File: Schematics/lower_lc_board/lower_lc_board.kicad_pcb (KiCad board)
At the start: 4 copper layers, 69.5 x 60 mm, 156 parts, among them J1 Conn_01x06, J10 SOL_CONN, J2 SWD_CONN, J3 USB_C_CONN, J4 HALL-1, J5 HALL-2, J6 PT1, J7 Screw_Terminal_01x02, J8 PT1, J9 SOL_CONN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

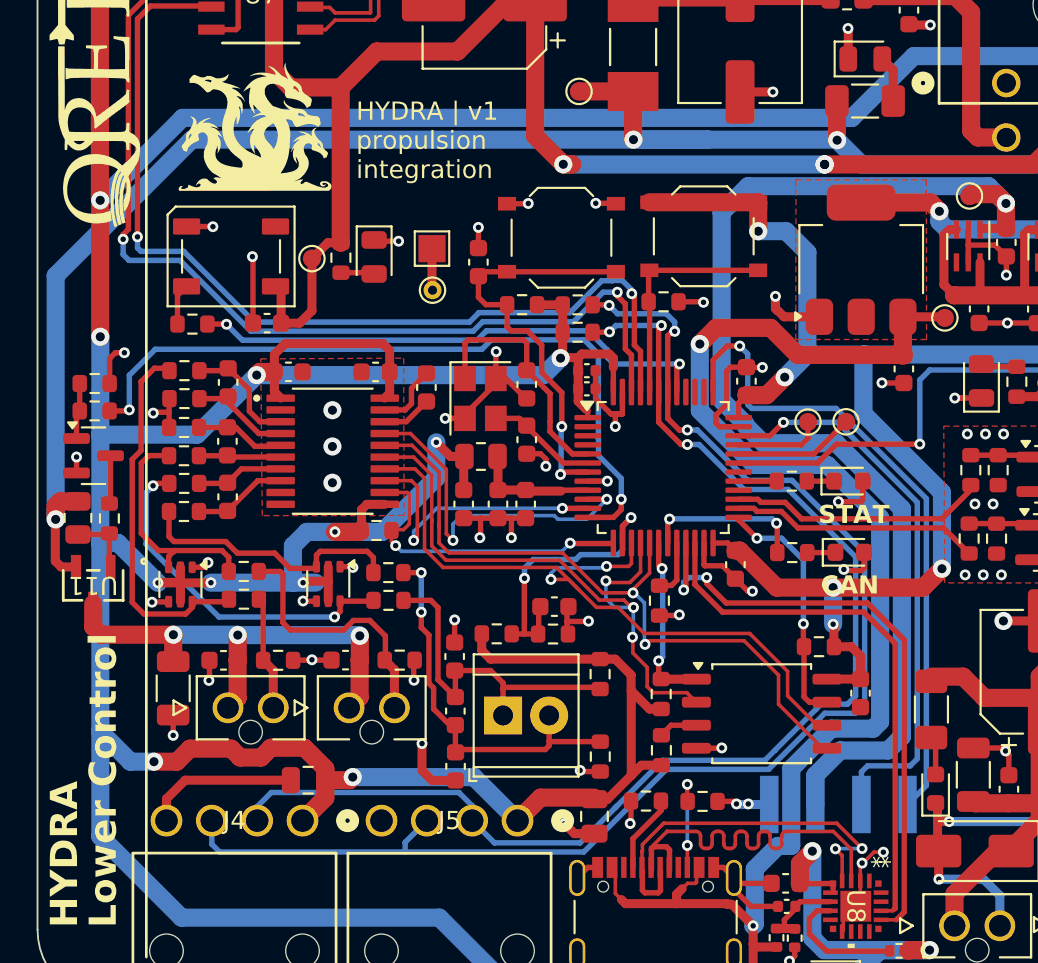
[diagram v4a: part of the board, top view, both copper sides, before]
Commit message: update with new TC screw terminal
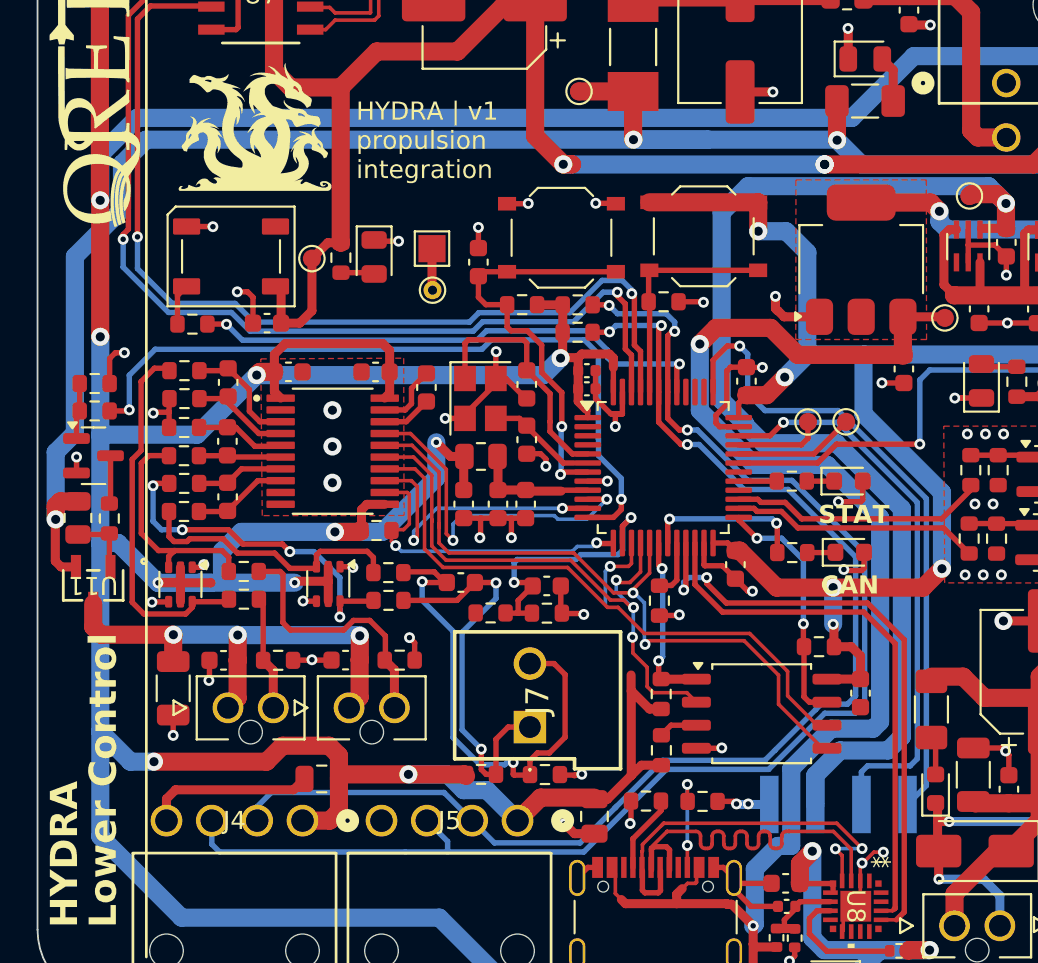
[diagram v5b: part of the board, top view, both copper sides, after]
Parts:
- removed C31, C32: 1nF, Capacitor_SMD:C_0603_1608Metric
- J7: footprint TerminalBlock_TE-Connectivity:TerminalBlock_TE_282834-2_1x02_P2.54mm_Horizontal -> SCREW-VERT:1984769
- moved R26 8.58 mm to (145.1, 95.0), turned to 0 degrees
- moved C30 7.10 mm to (143.9, 84.4), turned to 0 degrees
- moved R27 3.21 mm to (148.6, 95.0), turned to 0 degrees
- moved J7 1.61 mm to (147.8, 92.4), turned to 90 degrees
- moved C34 1.22 mm to (148.7, 84.6)
- moved R25 1.20 mm to (145.6, 86.1)
- moved TH1 1.20 mm to (148.7, 86.1)
- moved C23 0.75 mm to (136.3, 95.2)
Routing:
- net /Sensing Circuitry/TC_N_1: track 21.5 -> 28.0 mm
- net GND: track 173.6 -> 168.3 mm, vias 77 -> 75
- net SPI_SCLK: track 41.2 -> 37.9 mm, vias 2 -> 1
- net /Sensing Circuitry/TC_P_1: track 19.0 -> 22.1 mm, vias 0 -> 2
- net +3V3: track 468.7 -> 471.1 mm, vias 20 -> 19
- net +24V: track 125.9 -> 127.4 mm
- net SPI_MISO: track 34.0 -> 32.5 mm
- net CAN_RX: track 53.0 -> 53.6 mm
- net TEMP_SENSE: track 15.9 -> 15.3 mm
- net Net-(D18A-K3A4): track 19.2 -> 19.4 mm, vias 2 -> 4
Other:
- board text added: "V1.1? notes (2026-03-26) - new power/can/BP entry with molex conn - new molex connectors for solenoids/PTs - restarted design for overall organization - vertical screw term for TC *TODO - get reviewed & adjust - pours - silkscreen"

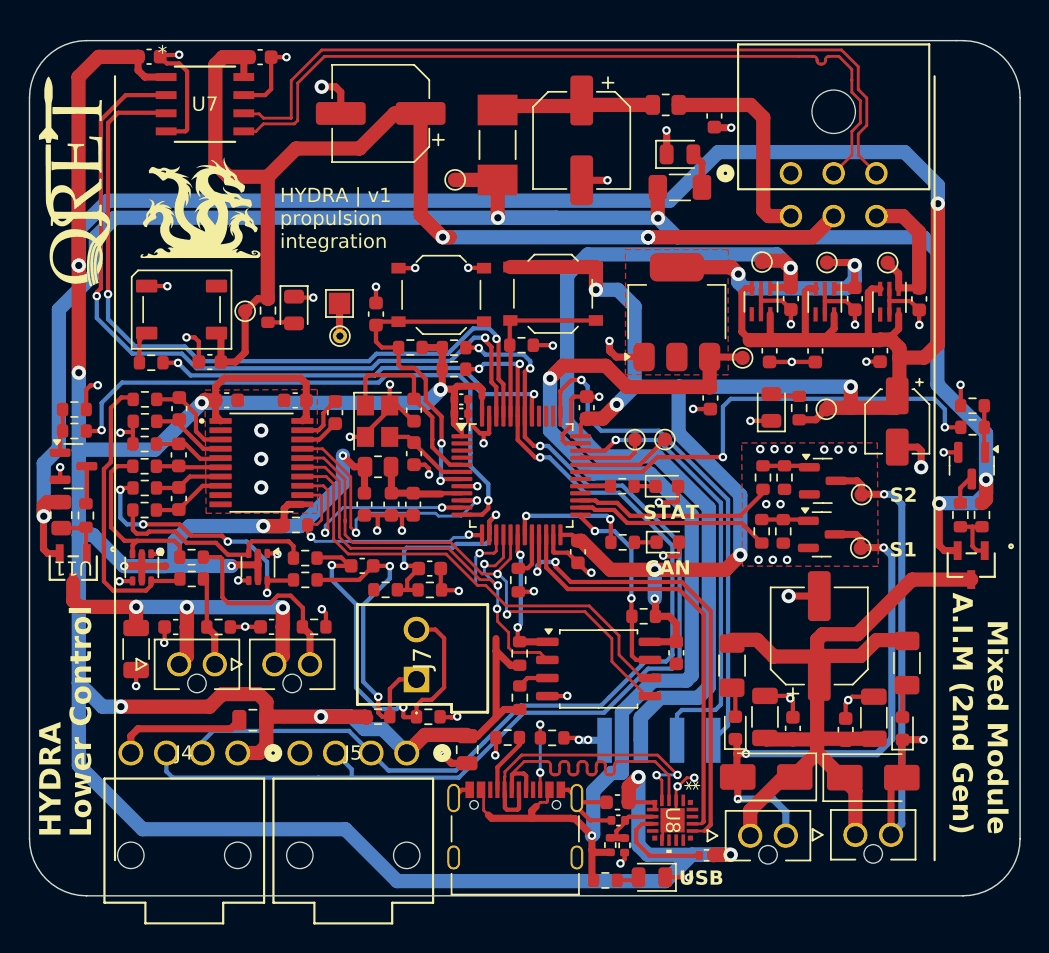
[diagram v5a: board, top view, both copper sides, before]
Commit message: update backplane orientation
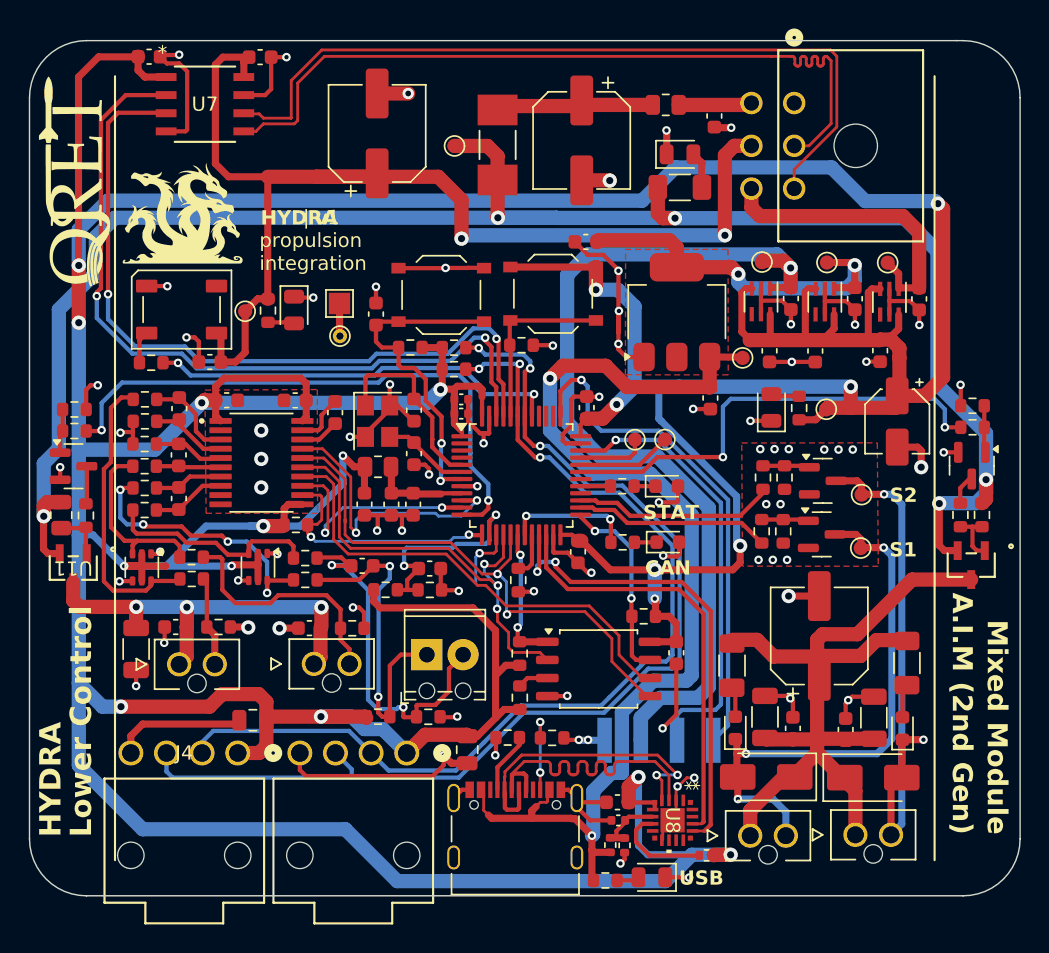
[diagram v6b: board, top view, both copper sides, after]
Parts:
- added C12: 10uF, Capacitor_SMD:C_0603_1608Metric, F.Cu at (159.6, 61.7)
- J7: footprint SCREW-VERT:1984769 -> TerminalBlock_Phoenix:TerminalBlock_Phoenix_MPT-0,5-2-2.54_1x02_P2.54mm_Horizontal
- moved J1 4.94 mm to (174.2, 51.9), turned to 90 degrees
- moved J8 2.77 mm to (140.6, 91.3)
- moved R35 2.68 mm to (143.2, 88.8)
- moved C36 2.66 mm to (140.2, 88.8)
- moved TP1 2.38 mm to (150.4, 54.9)
- moved J7 1.89 mm to (148.5, 90.6), turned to 0 degrees
- moved C4 1.42 mm to (145.0, 54.1), turned to 90 degrees
- moved G*** 1.31 mm to (131.4, 59.7)
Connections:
- net /Sensing Circuitry/PT1 renamed Net-(J6-Pin_2)
- net /Sensing Circuitry/PT2 renamed Net-(J8-Pin_2)
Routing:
- net GND: track 168.3 -> 199.6 mm, vias 75 -> 78
- net +3V3: track 471.1 -> 484.4 mm
- net /Power Circuitry/3V3_BP: track 10.9 -> 21.2 mm
- net +24V_BP: track 14.9 -> 4.72 mm
- net /Power Circuitry/3V3_USB: track 19.7 -> 26.9 mm
- net +24V: track 127.4 -> 130.4 mm
- net +5V: track 83.1 -> 80.3 mm, vias 3 -> 2
- net /Sensing Circuitry/VPT: track 26.1 -> 28.7 mm
- net Net-(J8-Pin_2): track 14.6 -> 17.0 mm
- net /Sensing Circuitry/TC_N_1: track 28.0 -> 26.0 mm
- net CAN_N: track 55.7 -> 57.5 mm
- net CAN_P: track 55.8 -> 57.5 mm
- net /Sensing Circuitry/TC_P_1: track 22.1 -> 23.7 mm
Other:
- board text added: "| v1 propulsion integration"
- board text removed: "HYDRA | v1 propulsion integration"

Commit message: PCB for review
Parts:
- removed C36, C8: 0.1uF, Capacitor_SMD:C_0603_1608Metric
- FB2: footprint Resistor_SMD:R_0805_2012Metric -> Resistor_SMD:R_0603_1608Metric
- U11, U12: footprint ul_SI2301CDS-T1-GE3:TO-236_VIS -> Package_TO_SOT_SMD:SOT-23
- moved C2 52.9 mm to (129.2, 88.1)
- moved FB1 52.5 mm to (126.7, 87.6)
- moved TP1 16.6 mm to (166.2, 60.0)
- moved C35 4.55 mm to (123.7, 88.9)
- moved C3 0.60 mm to (159.4, 54.0)
- turned U11 to -90 degrees
- turned U12 to -90 degrees
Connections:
- C2 pad 1: +24V_BP -> VPT
- C3 pad 1: Net-(C3-Pad1) -> +24V_BP
- C35 pad 1: /Sensing Circuitry/VPT -> Net-(U11-D)
- F1 pad 2: Net-(C3-Pad1) -> +24V_BP
- FB1 pad 1: +24V_BP -> VPT
- FB1 pad 2: Net-(C3-Pad1) -> Net-(U11-D)
- J6 pad 1: /Sensing Circuitry/VPT -> VPT
- J8 pad 1: /Sensing Circuitry/VPT -> VPT
- U11 pad 3: /Sensing Circuitry/VPT -> Net-(U11-D)
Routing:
- net /Sensing Circuitry/VPT: track 28.7 -> 0.00 mm, vias 3 -> 0
- net VPT: track 0.00 -> 20.3 mm, vias 0 -> 2
- net +24V_BP: track 4.72 -> 17.8 mm
- net Net-(C3-Pad1): track 11.3 -> 0.00 mm
- net +24V: track 130.4 -> 126.1 mm
- net Net-(U11-D): track 0.00 -> 4.03 mm
- net +3V3: track 484.4 -> 480.7 mm
- net CAN_N: track 57.5 -> 55.9 mm
- net CAN_P: track 57.5 -> 56.0 mm
- net GND: track 199.6 -> 200.4 mm, vias 78 -> 76
- net Net-(D13B-K1A2): track 12.9 -> 13.6 mm
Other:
- board text added: "DBG"
- board text removed: "STAT"

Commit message: WIP - i2c-2 refactor
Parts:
- removed TP7: USB-DM, TestPoint:TestPoint_Pad_D1.0mm
- removed TP8: USB-DP, TestPoint:TestPoint_Pad_D1.0mm
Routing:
- net Net-(U5-PA11): track 6.65 -> 0.00 mm
- net Net-(U5-PA12): track 4.87 -> 0.00 mm
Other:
- board text added: "V1.1? notes (2026-03-26) - new power/can/BP entry with molex conn - new molex connectors for solenoids/PTs - restarted design for overall organization - vertical screw term for TC *TODO - get reviewed & adjust - can termination resistor 120 ohm - 2nd i2c bus ffs - pours - silkscreen"
- board text removed: "V1.1? notes (2026-03-26) - new power/can/BP entry with molex conn - new molex connectors for solenoids/PTs - restarted design for overall organization - vertical screw term for TC *TODO - get reviewed & adjust - pours - silkscreen"
